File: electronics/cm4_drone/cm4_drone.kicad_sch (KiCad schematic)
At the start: 56 parts, among them J2 HDMI_A, J8 Conn_01x02_Female, J9 Conn_01x02_Female, U1 74LVC1G04, U3 ADS1115IDGS, U4 USB2514B_Bi, U6 TPS22948DCKR

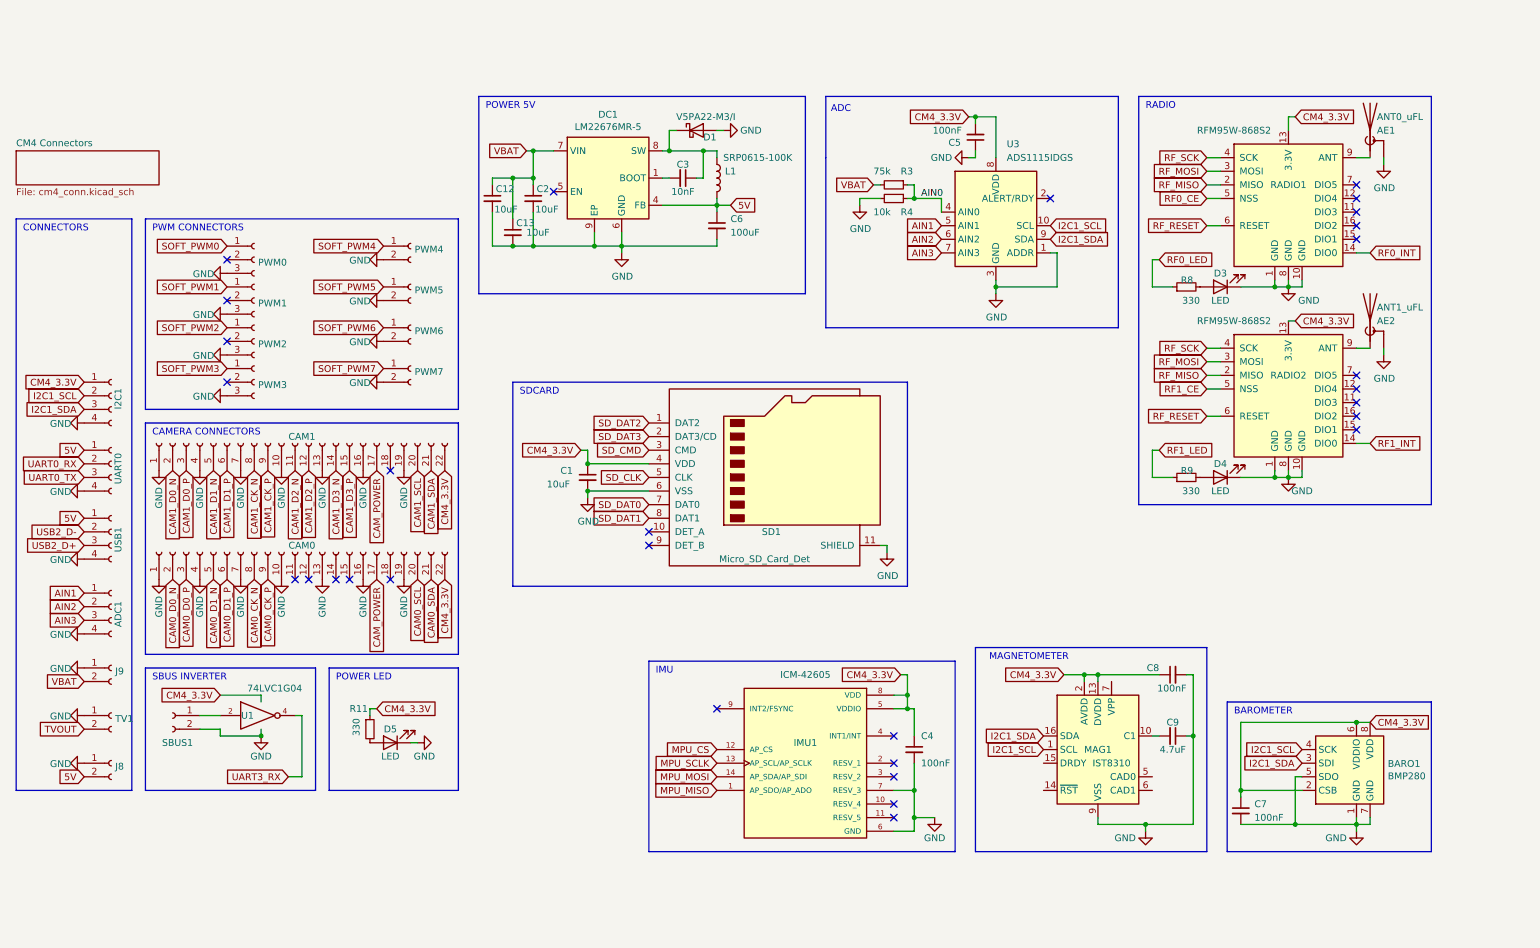
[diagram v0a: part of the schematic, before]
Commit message: new CM4 carrier board
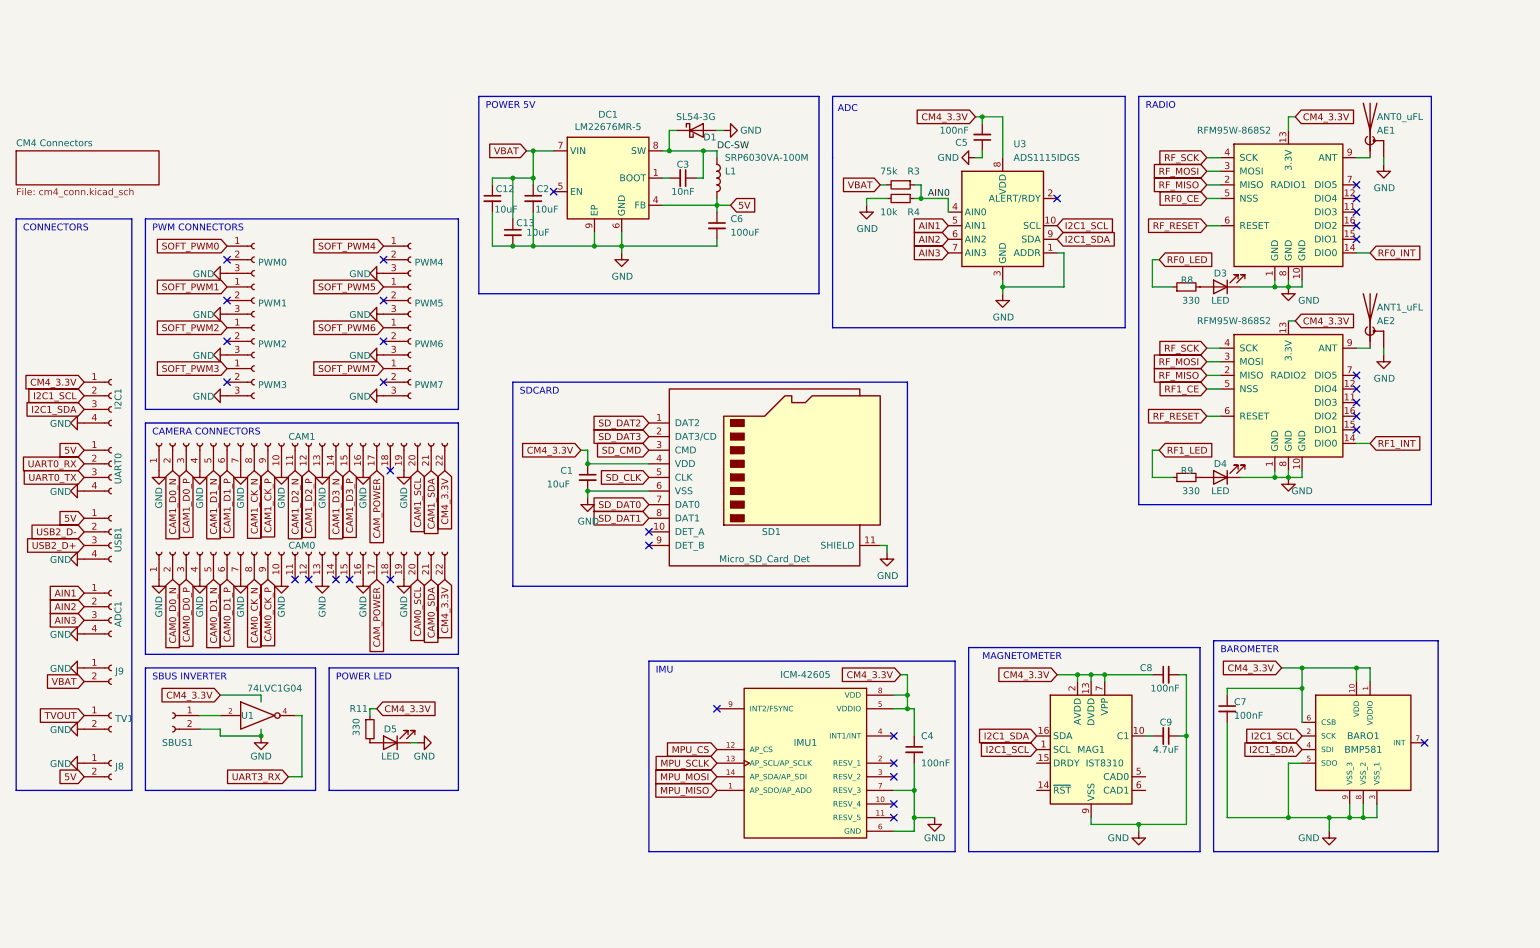
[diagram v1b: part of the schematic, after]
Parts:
- removed BARO1: BMP280, Package_LGA:Bosch_LGA-8_2x2.5mm_P0.65mm_ClockwisePinNumbering, symbol Sensor_Pressure:BMP280
- removed PWM4, PWM5, PWM6, PWM7: Conn_01x02_Female, cm4_drone:Breakout_1x02_2mm_SMD, symbol Connector:Conn_01x02_Female
- added BARO1: BMP581, footprints:BMP581, symbol BMP581:BMP581
- added PWM4, PWM5, PWM6, PWM7: Conn_01x03_Female, Connector_PinHeader_2.54mm:PinHeader_1x03_P2.54mm_Vertical, symbol Connector:Conn_01x03_Female
- D1: value V5PA22-M3/I -> SL54-3G; footprint Diode_SMD:D_2010_5025Metric -> Diode_SMD:D_SMB
- L1: value SRP0615-100K -> SRP6030VA-100M
- TV1: footprint cm4_drone:Breakout_1x02_2mm_SMD -> Connector_Coaxial:U.FL_Hirose_U.FL-R-SMT-1_Vertical
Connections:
- net GND: now also TV1.2 (Pin_2), BARO1.3 (VSS_1), BARO1.5 (SDO), BARO1.8 (VSS_2), BARO1.9 (VSS_3), PWM4.3 (Pin_3), PWM5.3 (Pin_3), PWM6.3 (Pin_3), PWM7.3 (Pin_3); no longer TV1.1 (Pin_1)
- net I2C1_SCL: now also BARO1.2 (SCK)
- net I2C1_SDA: now also BARO1.4 (SDI)
- net SOFT_PWM4: now also PWM4.1 (Pin_1)
- net SOFT_PWM5: now also PWM5.1 (Pin_1)
- net SOFT_PWM6: now also PWM6.1 (Pin_1)
- net SOFT_PWM7: now also PWM7.1 (Pin_1)
- net TVOUT: now also TV1.1 (Pin_1); no longer TV1.2 (Pin_2)
- net VCC: now also MAG1.7 (VPP), BARO1.1 (VDDIO), BARO1.10 (VDD), BARO1.6 (CSB)
- net DC-SW: now reaches C3.1, D1.1 (K), DC1.8 (SW), L1.1
- no-connect marks 32 -> 37
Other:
- moved on the sheet: C5, C7, C8, C9, MAG1, R3, R4, U3

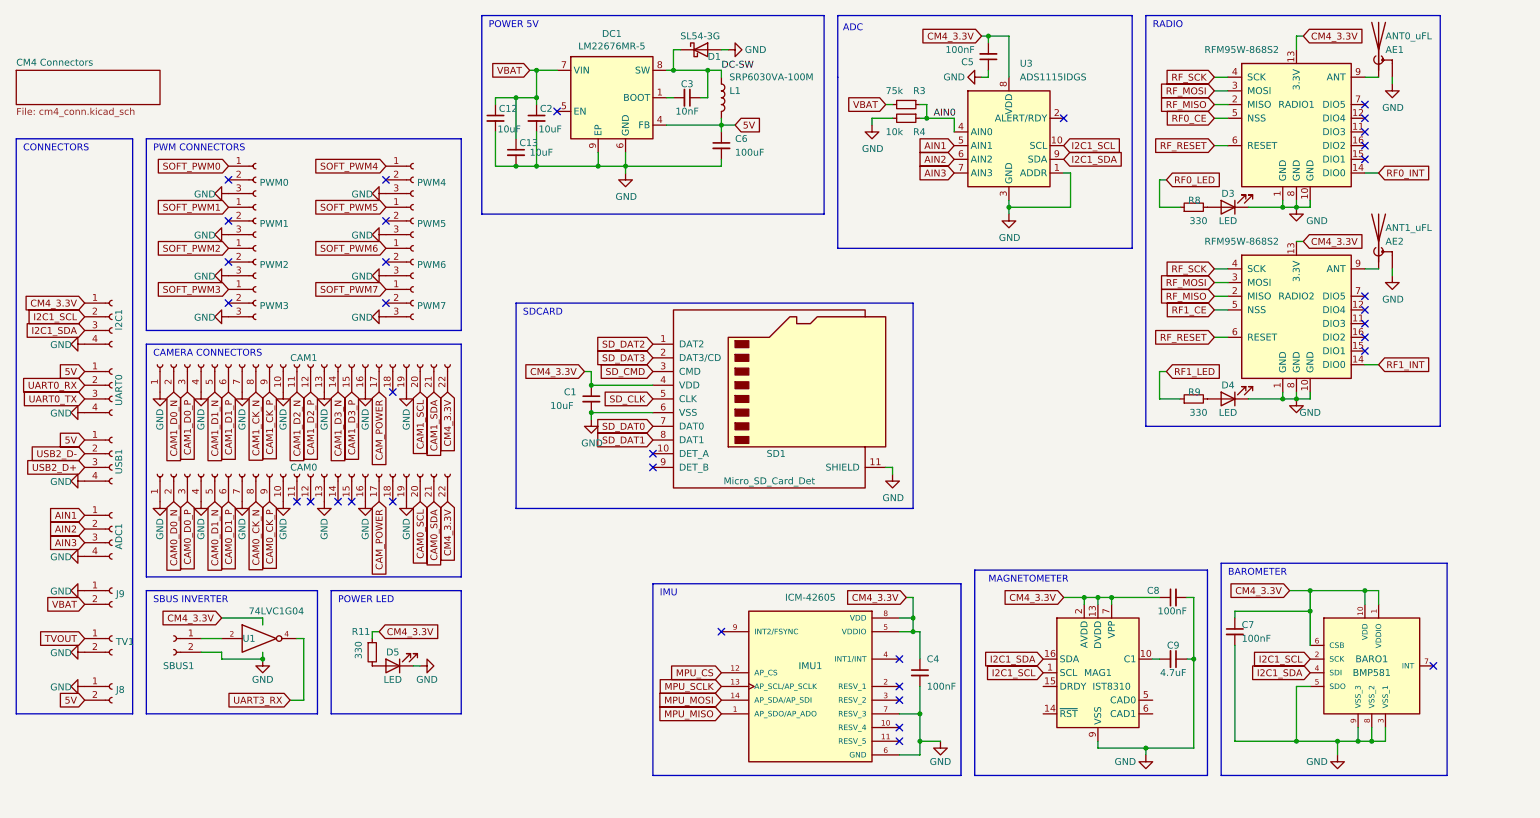
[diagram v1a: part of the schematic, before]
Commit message: electronics: fix labels shapes
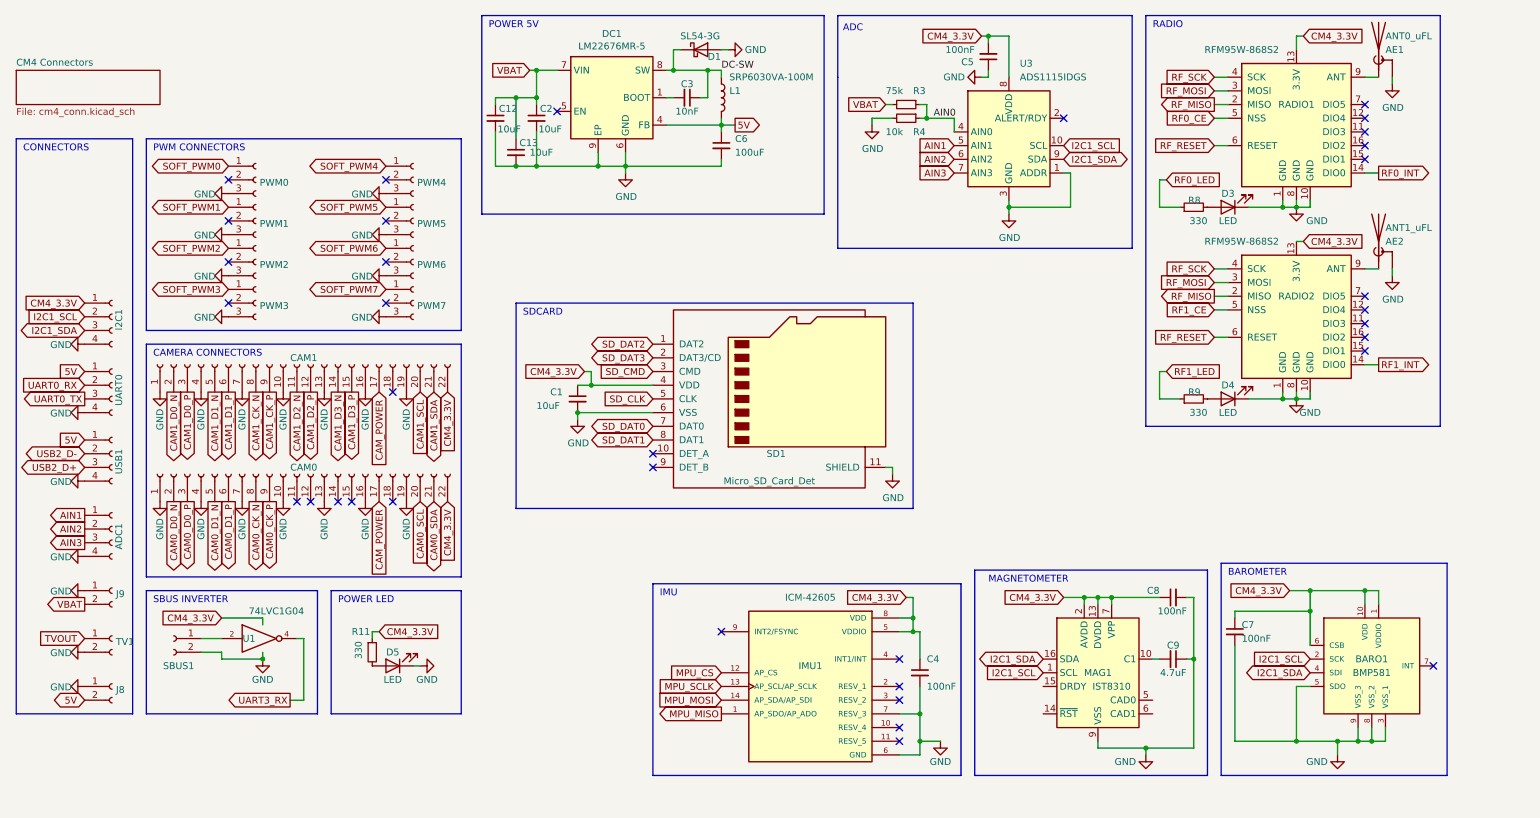
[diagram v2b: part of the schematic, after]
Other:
- moved on the sheet: C1

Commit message: electronics: add TVS diode to prevent battery spikes from frying voltage regulator
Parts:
- added D6: SMAJ36A, Diode_SMD:D_SMA, symbol Diode:SMAJ36A
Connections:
- net GND: now also D6.2 (A2)
- net VBAT: now also D6.1 (A1)
- net DC-SW: no longer names the net of C3.1, D1.1 (K), DC1.8 (SW), L1.1
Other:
- moved on the sheet: C12, C13, C2, PWM4, PWM5, PWM6, PWM7
